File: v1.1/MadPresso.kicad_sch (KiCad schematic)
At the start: 36 parts, among them J1 Conn_01x07, J2 Conn_01x03, J3 Conn_01x04, Q1 BSS84, Q3 BC847, U1 LTV-356T, U2 WeMos_D1_mini, U8 ADC101C021CIMK

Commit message: cleanups all over
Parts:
- added C11: DNP, Capacitor_SMD:C_0603_1608Metric_Pad1.08x0.95mm_HandSolder, symbol Device:C_Small
- added R31: 0R, Resistor_SMD:R_0603_1608Metric_Pad0.98x0.95mm_HandSolder, symbol Device:R_Small
- C1: footprint Capacitor_SMD:C_0603_1608Metric_Pad1.05x0.95mm_HandSolder -> Capacitor_SMD:C_0603_1608Metric_Pad1.08x0.95mm_HandSolder
- C2: renamed from C3; footprint Capacitor_SMD:C_0603_1608Metric_Pad1.05x0.95mm_HandSolder -> Capacitor_SMD:C_0603_1608Metric_Pad1.08x0.95mm_HandSolder
- C4: renamed from C8; footprint Capacitor_SMD:C_0603_1608Metric_Pad1.05x0.95mm_HandSolder -> Capacitor_SMD:C_0603_1608Metric_Pad1.08x0.95mm_HandSolder
- C5: renamed from C9; footprint Capacitor_SMD:C_0603_1608Metric_Pad1.05x0.95mm_HandSolder -> Capacitor_SMD:C_0603_1608Metric_Pad1.08x0.95mm_HandSolder
- C6: renamed from C10; footprint Capacitor_SMD:C_0603_1608Metric_Pad1.05x0.95mm_HandSolder -> Capacitor_SMD:C_0603_1608Metric_Pad1.08x0.95mm_HandSolder
- C7: renamed from C5; footprint Capacitor_SMD:C_0603_1608Metric_Pad1.05x0.95mm_HandSolder -> Capacitor_SMD:C_0603_1608Metric_Pad1.08x0.95mm_HandSolder
- F1: value 0.1A/250V -> 0.2A/250V
- R1: renamed from R3; footprint Resistor_SMD:R_1206_3216Metric_Pad1.42x1.75mm_HandSolder -> Resistor_SMD:R_1206_3216Metric_Pad1.30x1.75mm_HandSolder
- R10: renamed from R2; footprint Resistor_SMD:R_0603_1608Metric_Pad1.05x0.95mm_HandSolder -> Resistor_SMD:R_0603_1608Metric_Pad0.98x0.95mm_HandSolder
- R11: renamed from R31; footprint Resistor_SMD:R_0603_1608Metric_Pad1.05x0.95mm_HandSolder -> Resistor_SMD:R_0603_1608Metric_Pad0.98x0.95mm_HandSolder
- R12: renamed from R13; footprint Resistor_SMD:R_0603_1608Metric_Pad1.05x0.95mm_HandSolder -> Resistor_SMD:R_0603_1608Metric_Pad0.98x0.95mm_HandSolder
- R2: renamed from R4; footprint Resistor_SMD:R_1206_3216Metric_Pad1.42x1.75mm_HandSolder -> Resistor_SMD:R_1206_3216Metric_Pad1.30x1.75mm_HandSolder
- R3: renamed from R7; footprint Resistor_SMD:R_0603_1608Metric_Pad1.05x0.95mm_HandSolder -> Resistor_SMD:R_0603_1608Metric_Pad0.98x0.95mm_HandSolder
- R4: renamed from R9; footprint Resistor_SMD:R_0603_1608Metric_Pad1.05x0.95mm_HandSolder -> Resistor_SMD:R_0603_1608Metric_Pad0.98x0.95mm_HandSolder
- R5: renamed from R11; footprint Resistor_SMD:R_0603_1608Metric_Pad1.05x0.95mm_HandSolder -> Resistor_SMD:R_0603_1608Metric_Pad0.98x0.95mm_HandSolder
- R6: renamed from R12; footprint Resistor_SMD:R_0603_1608Metric_Pad1.05x0.95mm_HandSolder -> Resistor_SMD:R_0603_1608Metric_Pad0.98x0.95mm_HandSolder
- R7: renamed from R14; footprint Resistor_SMD:R_0603_1608Metric_Pad1.05x0.95mm_HandSolder -> Resistor_SMD:R_0603_1608Metric_Pad0.98x0.95mm_HandSolder
- R8: footprint Resistor_SMD:R_0603_1608Metric_Pad1.05x0.95mm_HandSolder -> Resistor_SMD:R_0603_1608Metric_Pad0.98x0.95mm_HandSolder
- R9: renamed from R1; footprint Resistor_SMD:R_0603_1608Metric_Pad1.05x0.95mm_HandSolder -> Resistor_SMD:R_0603_1608Metric_Pad0.98x0.95mm_HandSolder
- U2: renamed from U8; footprint Package_TO_SOT_SMD:SOT-23-6 -> Package_TO_SOT_SMD:SOT-23-6_Handsoldering
- renumbered C2 to C3, C4 to C8, D6 to D2, D9 to D3, D2 to D4, D8 to D5, Q3 to Q1, Q1 to Q2, U2 to U3
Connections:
- net ADC: now also C11.1
- net GND: now also C11.2, R31.2; no longer U2.4 (ADDR)
- net PUMP_TRIAC: now also U3.6 (MOSI/D7); no longer U3.12 (D3)
- net STEAM_SENSOR: now also U3.12 (D3); no longer U3.6 (MOSI/D7)
- new net: R31.1, U2.4 (ADDR)
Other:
- moved on the sheet: C1, C2, C3, C4, C5, C6, C7, D1, D2, D4, F1, J2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

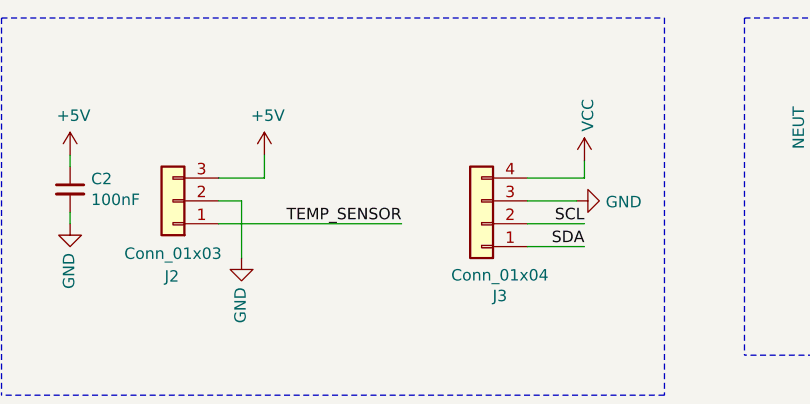
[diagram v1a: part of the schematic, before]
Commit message: start rework to smd triac
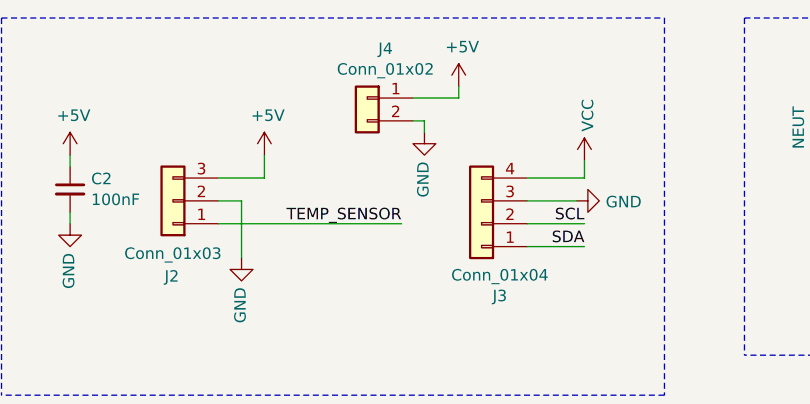
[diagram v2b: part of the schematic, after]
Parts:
- added J4: Conn_01x02, Connector_PinHeader_2.54mm:PinHeader_1x02_P2.54mm_Vertical, symbol Connector_Generic:Conn_01x02
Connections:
- net +5V: now also J4.1 (Pin_1)
- net GND: now also J4.2 (Pin_2)
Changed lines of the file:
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@@
+    (stroke (width 0) (type solid) (color 0 0 0 0))
+  )
+  (wire (pts (xy 139.7 25.4) (xy 144.78 25.4))
+    (stroke (width 0) (type solid) (color 0 0 0 0))
+  )
+  (wire (pts (xy 139.7 27.94) (xy 140.97 27.94))
+    (stroke (width 0) (type solid) (color 0 0 0 0))
+  )
+  (wire (pts (xy 140.97 27.94) (xy 140.97 29.21))
     (stroke (width 0) (type solid) (color 0 0 0 0))
   )
@@
   )
   (wire (pts (xy 143.51 157.48) (xy 146.05 157.48))
+    (stroke (width 0) (type solid) (color 0 0 0 0))
+  )
+  (wire (pts (xy 144.78 25.4) (xy 144.78 24.13))
     (stroke (width 0) (type solid) (color 0 0 0 0))
   )
@@
     )
   )
+  (symbol (lib_id "power:+5V") (at 144.78 24.13 0) (unit 1)
+    (in_bom yes) (on_board yes)
+    (property "Reference" "#PWR0102" (id 0) (at 144.78 27.94 0)
+      (effects (font (size 1.27 1.27)) hide)
+    )
+    (property "Value" "+5V" (id 1) (at 145.161 19.7358 0))
+    (property "Footprint" "" (id 2) (at 144.78 24.13 0)
+      (effects (font (size 1.27 1.27)) hide)
+    )
+    (property "Datasheet" "" (id 3) (at 144.78 24.13 0)
+      (effects (font (size 1.27 1.27)) hide)
+    )
+  )
   (symbol (lib_id "power:VCC") (at 158.75 32.385 0) (unit 1)
     (in_bom yes) (on_board yes)
@@
     )
     (property "Datasheet" "" (id 3) (at 134.62 91.44 0)
+      (effects (font (size 1.27 1.27)) hide)
+    )
+  )
+  (symbol (lib_id "power:GND") (at 140.97 29.21 0) (mirror y) (unit 1)
+    (in_bom yes) (on_board yes)
+    (property "Reference" "#PWR0103" (id 0) (at 140.97 35.56 0)
+      (effects (font (size 1.27 1.27)) hide)
+    )
+    (property "Value" "GND" (id 1) (at 140.843 32.4612 90)
+      (effects (font (size 1.27 1.27)) (justify right))
+    )
+    (property "Footprint" "" (id 2) (at 140.97 29.21 0)
+      (effects (font (size 1.27 1.27)) hide)
+    )
+    (property "Datasheet" "" (id 3) (at 140.97 29.21 0)
       (effects (font (size 1.27 1.27)) hide)
     )
@@
     )
     (property "Datasheet" "~" (id 3) (at 199.644 34.671 0)
+      (effects (font (size 1.27 1.27)) hide)
+    )
+  )
+  (symbol (lib_id "Connector_Generic:Conn_01x02") (at 134.62 25.4 0) (mirror y) (unit 1)
+    (in_bom yes) (on_board yes)
+    (property "Reference" "J4" (id 0) (at 136.652 19.9198 0))
+    (property "Value" "Conn_01x02" (id 1) (at 136.652 22.2185 0))
+    (property "Footprint" "Connector_PinHeader_2.54mm:PinHeader_1x02_P2.54mm_Vertical" (id 2) (at 134.62 25.4 0)
+      (effects (font (size 1.27 1.27)) hide)
+    )
+    (property "Datasheet" "~" (id 3) (at 134.62 25.4 0)
       (effects (font (size 1.27 1.27)) hide)
     )
@@
       (reference "#PWR0101") (unit 1) (value "GND") (footprint "")
     )
+    (path "/46df9f3d-c750-423c-8fa3-45d2657b799e"
+      (reference "#PWR0102") (unit 1) (value "+5V") (footprint "")
+    )
+    (path "/cdcf9d03-9b31-44b0-a1c0-74783c8f33a7"
+      (reference "#PWR0103") (unit 1) (value "GND") (footprint "")
+    )
     (path "/00000000-0000-0000-0000-00005ffbcb7d"
       (reference "C1") (unit 1) (value "1nF") (footprint "Capacitor_SMD:C_0603_1608Metric_Pad1.08x0.95mm_HandSolder")
@@
       (reference "J3") (unit 1) (value "Conn_01x04") (footprint "Connector_JST:JST_PH_S4B-PH-K_1x04_P2.00mm_Horizontal")
     )
+    (path "/7b0bb282-6da3-4213-acc3-6197a6536a13"
+      (reference "J4") (unit 1) (value "Conn_01x02") (footprint "Connector_PinHeader_2.54mm:PinHeader_1x02_P2.54mm_Vertical")
+    )
     (path "/d88f3030-1974-43e3-8892-faa2a80ca689"
       (reference "PS1") (unit 1) (value "HLK-PM01") (footprint "Converter_ACDC:Converter_ACDC_HiLink_HLK-PMxx")
@@
     )
     (path "/00000000-0000-0000-0000-000060629c35/00000000-0000-0000-0000-00006062f252"
-      (reference "Q3") (unit 1) (value "BT138-600") (footprint "Package_TO_SOT_THT:TO-220-3_Vertical")
+      (reference "Q3") (unit 1) (value "BT138-600") (footprint "Package_TO_SOT_SMD:TO-252-2")
     )
     (path "/00000000-0000-0000-0000-000060629c35/00000000-0000-0000-0000-00006062f258"
@@
     )
     (path "/00000000-0000-0000-0000-00006068f3b5/00000000-0000-0000-0000-00006062f252"
-      (reference "Q5") (unit 1) (value "BT138-600") (footprint "Package_TO_SOT_THT:TO-220-3_Vertical")
+      (reference "Q5") (unit 1) (value "BT138-600") (footprint "Package_TO_SOT_SMD:TO-252-2")
     )
     (path "/00000000-0000-0000-0000-00006068f3b5/00000000-0000-0000-0000-00006062f258"
@@
     )
     (path "/00000000-0000-0000-0000-0000606d3a29/00000000-0000-0000-0000-00006062f252"
-      (reference "Q7") (unit 1) (value "BT138-600") (footprint "Package_TO_SOT_THT:TO-220-3_Vertical")
+      (reference "Q7") (unit 1) (value "BT138-600") (footprint "Package_TO_SOT_SMD:TO-252-2")
     )
     (path "/00000000-0000-0000-0000-0000606d3a29/00000000-0000-0000-0000-00006062f258"

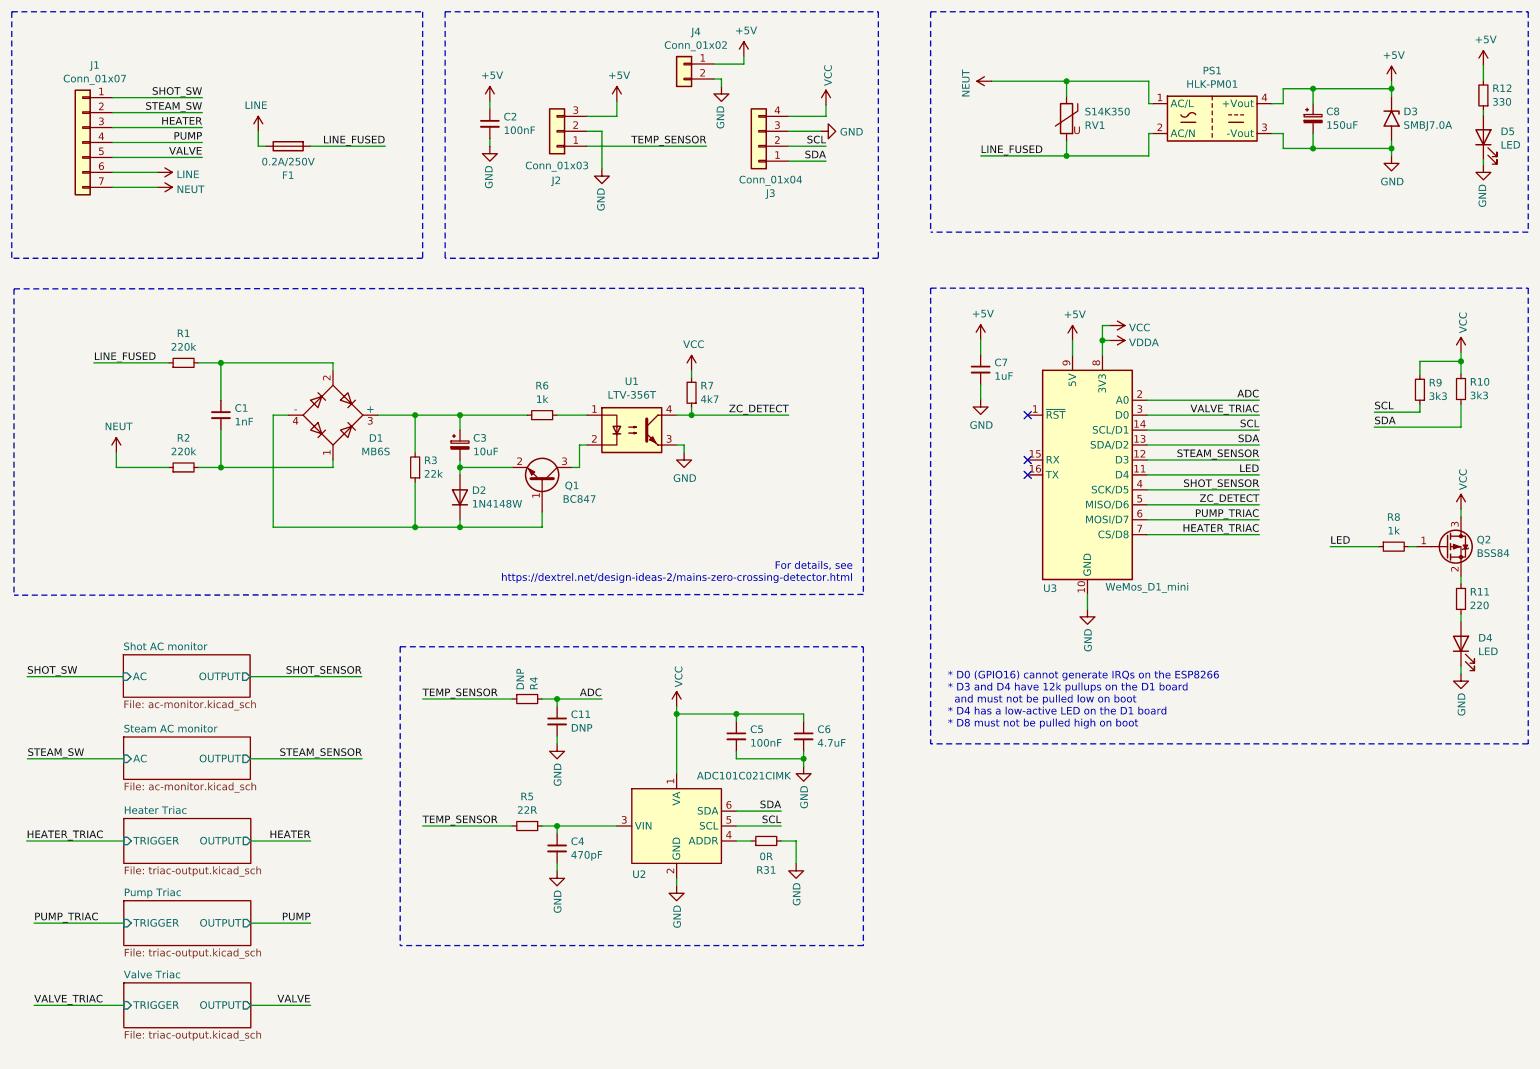
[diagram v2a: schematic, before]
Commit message: more work on smd triac routing
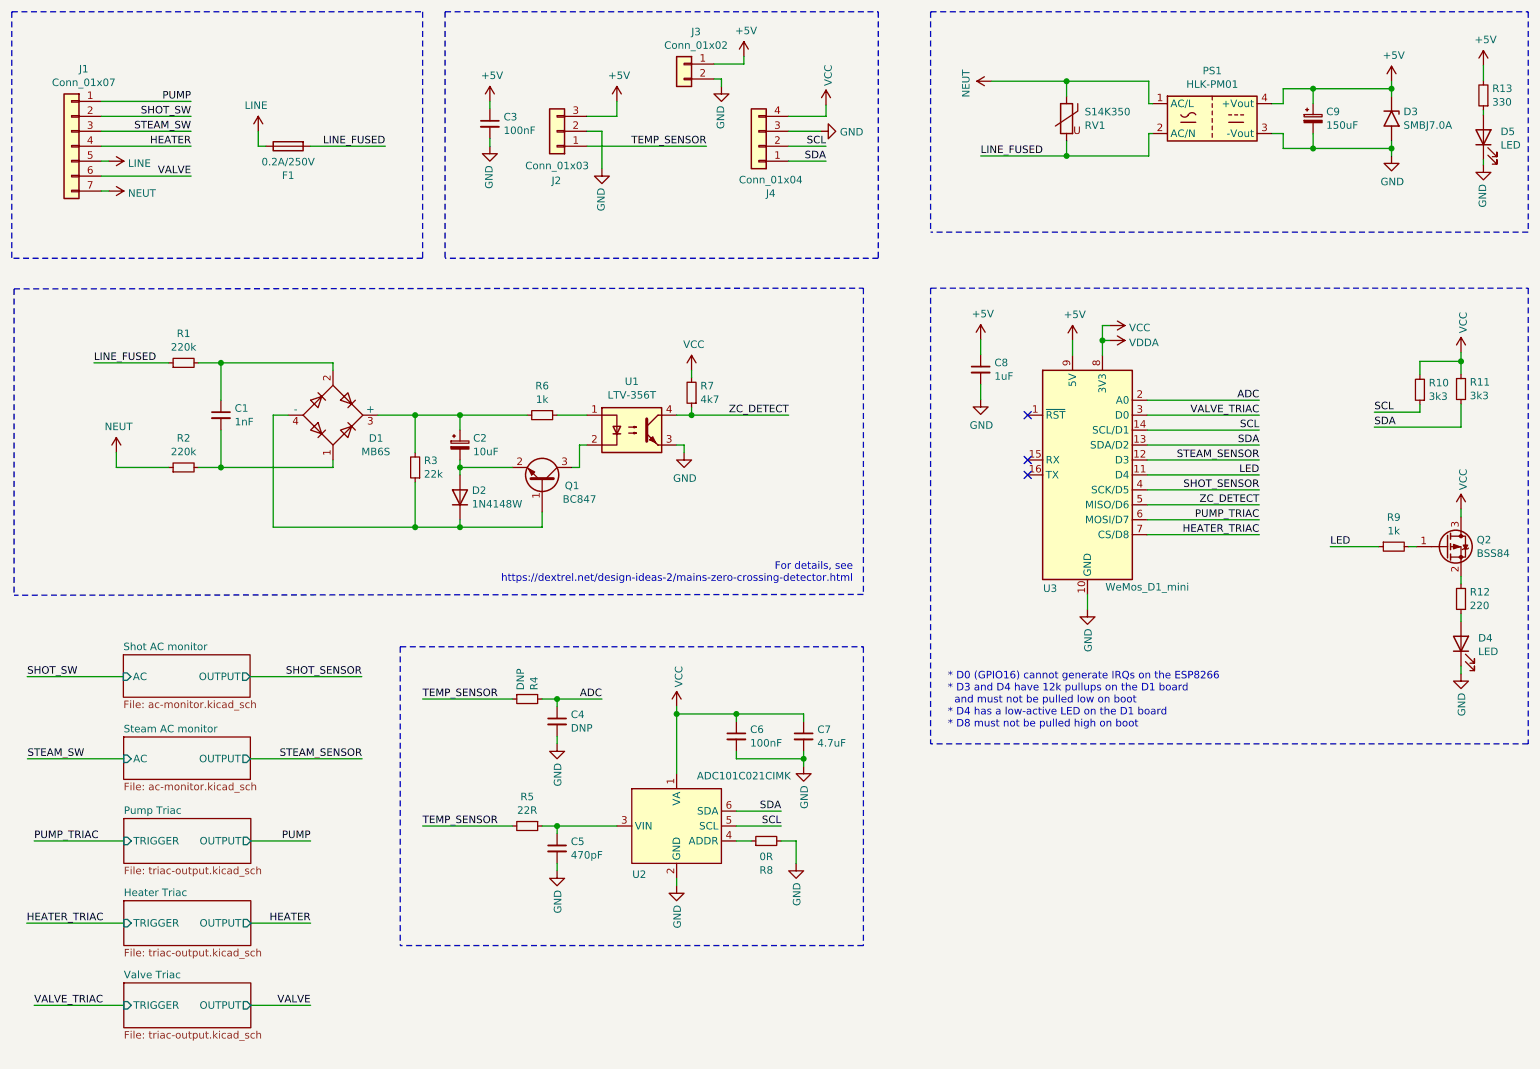
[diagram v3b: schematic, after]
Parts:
- renumbered C3 to C2, C2 to C3, C11 to C4, C4 to C5, C5 to C6, C6 to C7, C7 to C8, C8 to C9, J4 to J3, J3 to J4, R9 to R10, R10 to R11, R11 to R12, R12 to R13, R31 to R8, R8 to R9
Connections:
- net HEATER: now also J1.4 (Pin_4); no longer J1.3 (Pin_3)
- net LINE: now also J1.5 (Pin_5); no longer J1.6 (Pin_6)
- net PUMP: now also J1.1 (Pin_1); no longer J1.4 (Pin_4)
- net SHOT_SW: now also J1.2 (Pin_2); no longer J1.1 (Pin_1)
- net STEAM_SW: now also J1.3 (Pin_3); no longer J1.2 (Pin_2)
- net VALVE: now also J1.6 (Pin_6); no longer J1.5 (Pin_5)
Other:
- moved on the sheet: J1

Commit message: more routing
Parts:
- added FID1, FID2, FID3: Fiducial, Fiducial:Fiducial_0.5mm_Mask1mm, symbol Mechanical:Fiducial
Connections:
- net HEATER: now also J1.6 (Pin_6); no longer J1.4 (Pin_4)
- net VALVE: now also J1.4 (Pin_4); no longer J1.6 (Pin_6)
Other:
- moved on the sheet: C9, D3, D5, PS1, R13, RV1

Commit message: more routing
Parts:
- R8: value 0R -> DNP
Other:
- note added: "I²C address pin: floating 0x50 GND 0x51 VA 0x52"
- title: (none) -> MadPresso controller
- moved on the sheet: C3, C4, C5, C6, C7, C9, D3, D5, F1, J1, J2, J3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

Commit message: some more documentation
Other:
- note added: "Connector for LM35DT"
- note added: "General purpose connectors (eg, OLED)"
- moved on the sheet: C1, C2, C3, C4, C5, C6, C7, D1, D2, F1, FID1, FID2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

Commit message: v1.1a
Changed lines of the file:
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@@
   (junction (at 255.27 41.91) (diameter 1.016) (color 0 0 0 0))
   (junction (at 266.7 75.946) (diameter 1.016) (color 0 0 0 0))
-  (no_connect (at 193.04 95.25))
   (no_connect (at 193.04 85.09))
   (no_connect (at 193.04 92.71))
+  (no_connect (at 193.04 95.25))
   (wire (pts (xy 22.86 184.15) (xy 39.37 184.15))
     (stroke (width 0) (type solid) (color 0 0 0 0))
@@
     (stroke (width 0) (type solid) (color 0 0 0 0))
   )
-  (wire (pts (xy 133.35 130.81) (xy 133.35 140.97))
+  (wire (pts (xy 133.35 130.81) (xy 133.35 142.24))
     (stroke (width 0) (type solid) (color 0 0 0 0))
   )
@@
     (stroke (width 0) (type solid) (color 0 0 0 0))
   )
-  (wire (pts (xy 133.35 158.75) (xy 133.35 160.02))
+  (wire (pts (xy 133.35 157.48) (xy 133.35 160.02))
     (stroke (width 0) (type solid) (color 0 0 0 0))
   )
@@
     (stroke (width 0) (type dash) (color 0 0 0 0))
   )
-  (polyline (pts (xy 20.701 63.627) (xy 20.701 114.427))
-    (stroke (width 0) (type dash) (color 0 0 0 0))
-  )
-  (polyline (pts (xy 20.701 63.627) (xy 165.1 63.5))
+  (polyline (pts (xy 20.32 63.5) (xy 20.32 114.3))
+    (stroke (width 0) (type dash) (color 0 0 0 0))
+  )
+  (polyline (pts (xy 20.32 63.5) (xy 165.1 63.5))
     (stroke (width 0) (type dash) (color 0 0 0 0))
   )
@@
     (stroke (width 0) (type dash) (color 0 0 0 0))
   )
-  (polyline (pts (xy 165.1 114.3) (xy 20.701 114.427))
-    (stroke (width 0) (type dash) (color 0 0 0 0))
-  )
+  (polyline (pts (xy 165.1 114.3) (xy 20.32 114.3))
+    (stroke (width 0) (type dash) (color 0 0 0 0))
+  )
